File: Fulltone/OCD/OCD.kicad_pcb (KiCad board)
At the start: 2 copper layers, 37 parts, among them J1 I/O, J2 Power, J3 Power, Q1 2N7000, Q2 2N7000, SW1 SW_SPDT, U1 TL082

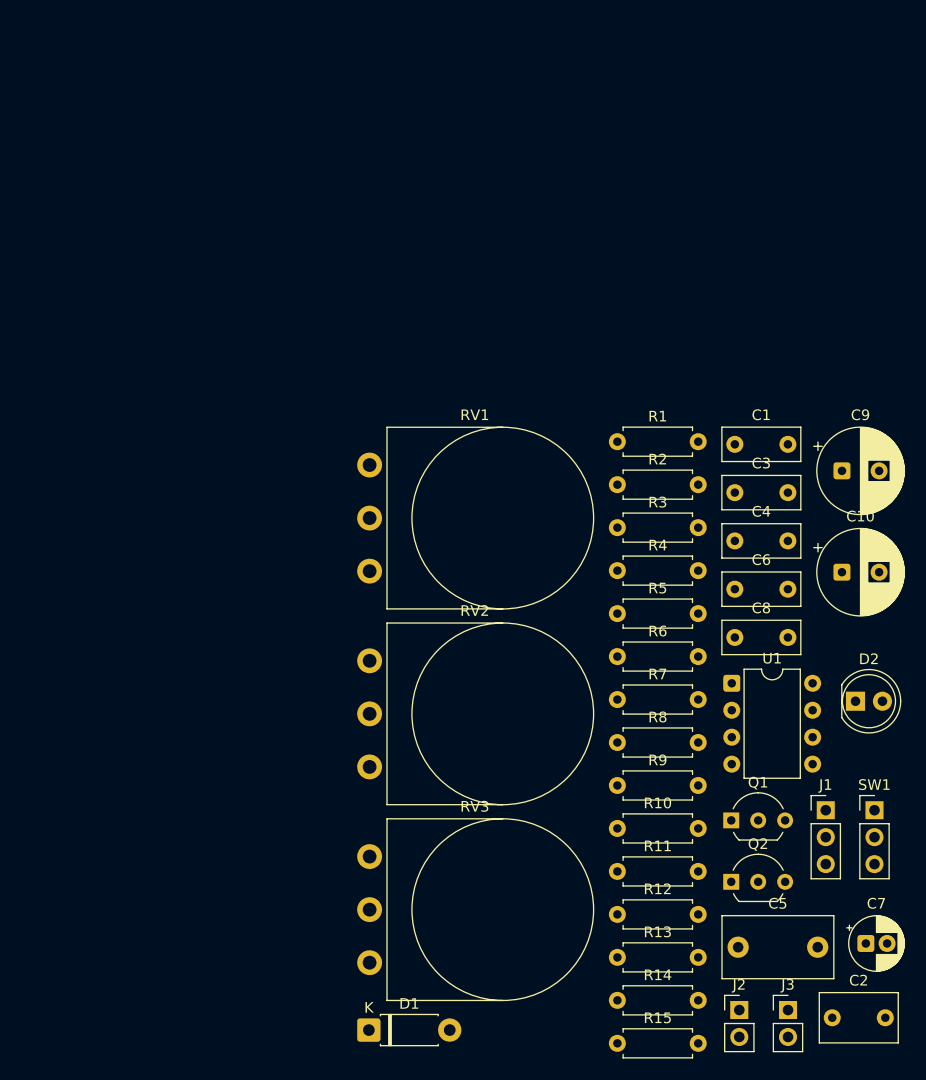
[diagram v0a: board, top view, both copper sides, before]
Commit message: feat: ReLayout Fulltone/OCD v3
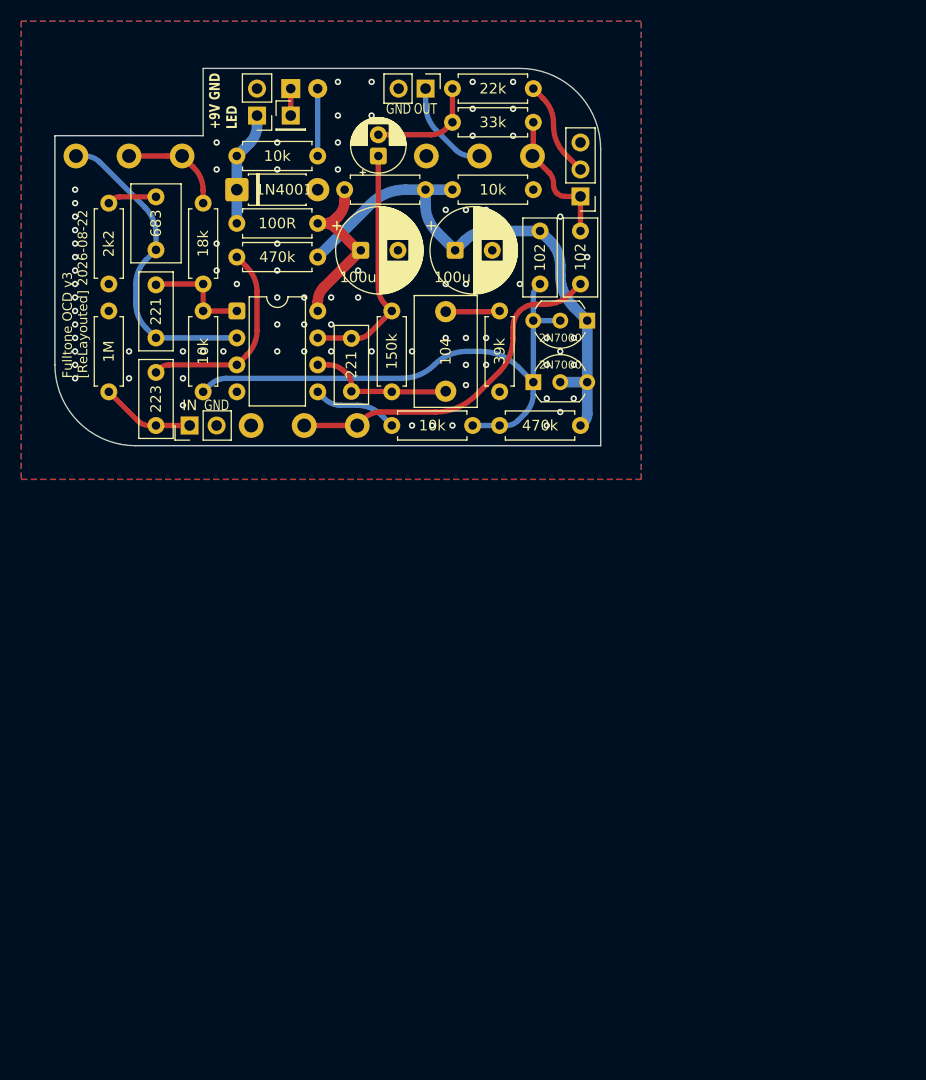
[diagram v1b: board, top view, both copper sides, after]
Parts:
- removed the J3 at (142.5, 131.3)
- added J4: LED, Connector_PinHeader_2.54mm:PinHeader_1x01_P2.54mm_Vertical, F.Cu at (95.6, 47.0)
- added J5: OUTPUT, Connector_PinHeader_2.54mm:PinHeader_1x02_P2.54mm_Vertical, F.Cu at (108.3, 44.5)
- C4: renamed from C3; value 220p -> 221
- C8: renamed from C6; value 220p -> 221
- D2, RV1, RV2, RV3: moved to B.Cu
- J1: value I/O -> INPUT; footprint Connector_PinHeader_2.54mm:PinHeader_1x03_P2.54mm_Vertical -> Connector_PinHeader_2.54mm:PinHeader_1x02_P2.54mm_Vertical
- J3: renamed from J2; value Power -> +9V
- moved C2 100.2 mm to (82.9, 54.6), turned to -90 degrees
- moved J3 95.8 mm to (92.4, 47.0), turned to 180 degrees
- moved C9 87.3 mm to (103.9, 50.8), turned to 90 degrees
- moved R5 83.6 mm to (90.5, 50.8)
- moved R7 80.8 mm to (118.5, 54.0), turned to 180 degrees
- moved R6 80.6 mm to (100.7, 54.0)
- moved D1 80.2 mm to (90.5, 54.0)
- moved D2 78.5 mm to (95.6, 44.5)
- moved RV3 76.2 mm to (108.4, 50.8), turned to 90 degrees
- moved R4 74.3 mm to (90.5, 57.1)
- moved R15 72.3 mm to (110.9, 47.6)
- moved R14 71.4 mm to (110.9, 44.5)
- moved J1 70.1 mm to (86.1, 76.2), turned to 90 degrees
- moved C7 65.9 mm to (110.2, 65.5), turned to -90 degrees
- moved SW1 64.1 mm to (122.9, 54.6), turned to 180 degrees
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- renumbered C8 to C10, C9 to C3, C10 to C5, C4 to C6, C5 to C7, C7 to C9, R6 to R10, R7 to R11, R8 to R12, R9 to R13, R10 to R14, R11 to R15, R12 to R4, R13 to R5, R14 to R6, R15 to R7, R4 to R8, R5 to R9
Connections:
- C10 pad 1: Net-(SW1-C) -> Net-(SW1-A)
- C10 pad 2: Net-(C8-Pad2) (its old number) -> Net-(C10-Pad2)
- J1 pad 2: /OUTPUT -> GND
- R15 pad 2: Net-(SW1-C) -> Net-(SW1-A)
- RV2 pad 1: Net-(C8-Pad2) (its old number) -> GND
- RV2 pad 2: GND -> Net-(C10-Pad2)
- RV2 pad 3: GND -> Net-(C10-Pad2)
- RV3 pad 3: Net-(SW1-C) -> Net-(SW1-A)
- SW1 pad 1: unconnected-(SW1-A-Pad1) -> Net-(SW1-A)
- SW1 pad 3: Net-(SW1-C) -> unconnected-(SW1-C-Pad3)
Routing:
- net Net-(Q1-D): track 0.00 -> 54.3 mm
- net NEUT: track 0.00 -> 53.0 mm
- net Net-(C10-Pad2): track 0.00 -> 32.8 mm
- net Net-(U1A--): track 0.00 -> 29.9 mm
- net Net-(C8-Pad2): track 0.00 -> 22.8 mm
- net Net-(U1A-+): track 0.00 -> 19.4 mm
- net Net-(U1C-V+): track 0.00 -> 17.3 mm
- net Net-(U1B--): track 0.00 -> 13.4 mm
- net Net-(SW1-A): track 0.00 -> 13.1 mm
- net +9V: track 0.00 -> 10.8 mm
- net Net-(C9-Pad2): track 0.00 -> 10.5 mm
- net Net-(C4-Pad2): track 0.00 -> 10.3 mm
- net Net-(R8-Pad1): track 0.00 -> 9.96 mm
- net /OUTPUT: track 0.00 -> 9.16 mm
- net Net-(SW1-B): track 0.00 -> 9.12 mm
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- added copper zone on B.Cu, net GND
- added copper zone on F.Cu, net GND
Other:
- board outline added: 51.4 x 35.6 mm
- board text added: "+9V GND LED"
- board text added: "Fulltone OCD v3 [ReLayouted] 2026-08-22"
- board text added: "GND"
- board text added: "IN"
- board text added: "OUT"

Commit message: fix: コンデンサの定数を修正
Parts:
- C10: value 102 -> 473
- renumbered J5 to J1, J1 to J2
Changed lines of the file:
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@@
 		(descr "Through hole straight pin header, 1x02, 2.54mm pitch, single row")
 		(tags "Through hole pin header THT 1x02 2.54mm single row")
-		(property "Reference" "J1"
+		(property "Reference" "J2"
 			(at 0 -2.38 90)
 			(layer "F.SilkS")
@@
 			)
 		)
-		(property "Value" "102"
+		(property "Value" "473"
 			(at 2.46 0 90)
 			(layer "F.SilkS")
@@
 		(descr "Through hole straight pin header, 1x02, 2.54mm pitch, single row")
 		(tags "Through hole pin header THT 1x02 2.54mm single row")
-		(property "Reference" "J5"
+		(property "Reference" "J1"
 			(at 0 -2.38 90)
 			(layer "F.SilkS")

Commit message: fix: 何らかの修正
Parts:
- renumbered J2 to J1, J1 to J2
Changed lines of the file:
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@@
 		(descr "Through hole straight pin header, 1x02, 2.54mm pitch, single row")
 		(tags "Through hole pin header THT 1x02 2.54mm single row")
-		(property "Reference" "J2"
+		(property "Reference" "J1"
 			(at 0 -2.38 90)
 			(layer "F.SilkS")
@@
 		(descr "Through hole straight pin header, 1x02, 2.54mm pitch, single row")
 		(tags "Through hole pin header THT 1x02 2.54mm single row")
-		(property "Reference" "J1"
+		(property "Reference" "J2"
 			(at 0 -2.38 90)
 			(layer "F.SilkS")
